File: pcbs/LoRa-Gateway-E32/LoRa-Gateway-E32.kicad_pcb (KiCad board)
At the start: 2 copper layers, 65.4 x 63 mm, 12 parts, among them J1 Conn_01x02, U1 ESP32_DevKit_V1_DOIT, U2 E-Byte-E32-900M20S, U3 QuinLED-ESP32-ETH-Hat

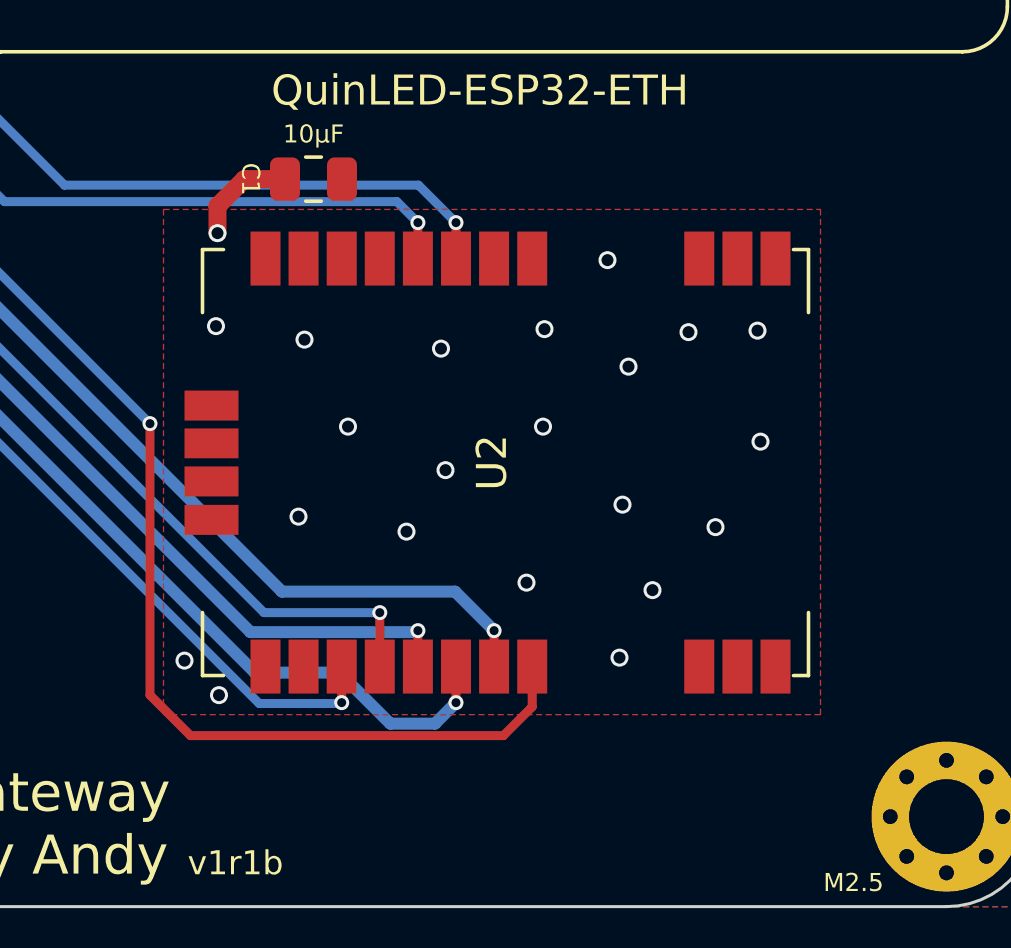
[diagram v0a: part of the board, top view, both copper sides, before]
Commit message: Added iBOM, last small edits on both PCBs
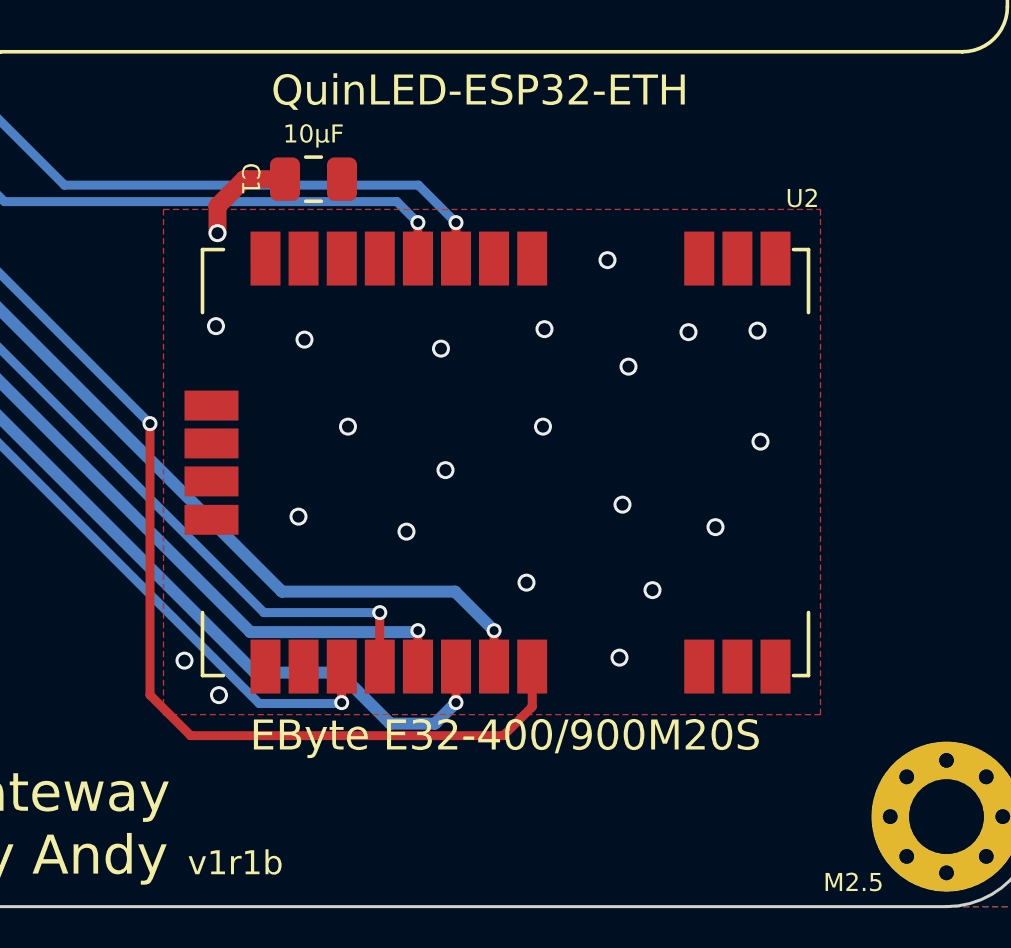
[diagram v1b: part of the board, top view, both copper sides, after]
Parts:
- U2: value E-Byte-E32-900M20S -> EByte E32-400/900M20S
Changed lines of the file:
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@@
   )
   (paper "A4")
+  (title_block
+    (title "LoRa-Gateway-E32")
+    (rev "v1r1b")
+  )
   (layers
     (0 "F.Cu" signal)
@@
     (property "Sheetname" "")
     (attr smd)
-    (fp_text reference "U2" (at 8.4 10.95 90) (layer "F.SilkS")
-      (effects (font (size 1 1) (thickness 0.15)))
-    )
-    (fp_text value "E-Byte-E32-900M20S" (at 8.4 22.8 90) (layer "F.Fab")
-      (effects (font (size 1 1) (thickness 0.15)))
+    (fp_text reference "U2" (at 17.1975 21.3 180) (layer "F.SilkS")
+      (effects (font (size 0.6 0.6) (thickness 0.12)))
+    )
+    (fp_text value "EByte E32-400/900M20S" (at -0.7025 11.4 180) (layer "F.SilkS")
+      (effects (font (size 1 1) (thickness 0.2)))
     )
     (fp_line (start 1.3 21.5) (end 1.3 21) (layer "F.SilkS") (width 0.12))
@@
     (fp_line (start -2.25 -1.6) (end 2.25 -1.6) (layer "F.Fab") (width 0.1))
     (fp_line (start 2.25 -1.6) (end 2.25 1.6) (layer "F.Fab") (width 0.1))
-    (pad "1" smd roundrect locked (at -2.1375 0 270) (size 1.125 3.4) (layers "F.Cu" "F.Paste" "F.Mask") (roundrect_rratio 0.2222222222)
+    (pad "1" smd roundrect (at -2.1375 0 270) (size 1.125 3.4) (layers "F.Cu" "F.Paste" "F.Mask") (roundrect_rratio 0.2222222222)
       (net 29 "5vF") (pintype "passive"))
-    (pad "2" smd roundrect locked (at 2.1375 0 270) (size 1.125 3.4) (layers "F.Cu" "F.Paste" "F.Mask") (roundrect_rratio 0.2222222222)
+    (pad "2" smd roundrect (at 2.1375 0 270) (size 1.125 3.4) (layers "F.Cu" "F.Paste" "F.Mask") (roundrect_rratio 0.2222222222)
       (net 30 "/5V") (pintype "passive"))
-    (model "${KICAD6_3DMODEL_DIR}/Fuse.3dshapes/Fuse_1812_4532Metric.wrl"
+    (model "${KICAD6_3DMODEL_DIR}/Fuse.3dshapes/Fuse_1812_4532Metric.wrl" hide
       (offset (xyz 0 0 0))
       (scale (xyz 1 1 1))
       (rotate (xyz 0 0 0))
     )
+    (model "${KICAD6_3DMODEL_DIR}/Fuse.3dshapes/Fuse_0805_2012Metric.wrl"
+      (offset (xyz 0 0 0))
+      (scale (xyz 2.5 2.5 2.5))
+      (rotate (xyz 0 0 0))
+    )
